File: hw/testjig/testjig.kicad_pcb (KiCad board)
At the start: 2 copper layers, 157.5 x 115.8 mm, 99 parts, among them J1 Conn_02x08_Odd_Even, J10 Conn_01x01, J11 Conn_01x01, J12 Conn_01x01, J13 Conn_01x01, J14 Conn_01x01, J15 Conn_01x01, J16 Conn_01x01, J17 Conn_01x01, J18 Conn_01x01, J19 Conn_01x01, J2 Conn_01x01, J20 Conn_01x04_Female, J21 Conn_01x01, J22 Conn_01x01, J23 Conn_01x01, J24 Conn_01x01, J25 Conn_01x01, J26 Conn_01x01, J27 Conn_01x01, J28 Conn_01x01, J29 Conn_01x01, J3 Conn_01x01, J30 Conn_01x01, J31 Conn_01x01, J32 Conn_01x01, J33 Conn_01x01, J34 Conn_01x01, J35 Conn_01x01, J36 Conn_01x01, J37 Conn_01x01, J38 Conn_01x01, J39 Conn_01x01, J4 Conn_01x01, J40 Conn_01x01, J41 Conn_01x01, J42 Conn_01x01, J43 Conn_02x08_Odd_Even, J44 USB_B_Micro, J45 Conn_02x07_Odd_Even, J46 Conn_01x04_Female, J47 Conn_01x06_Female, J48 Conn_01x02_Female, J49 Conn_01x01, J5 Conn_01x01, J50 Conn_01x01, J51 SJ1-3523N-cap, J6 Conn_01x01, J7 Conn_01x01, J8 Conn_01x01, J9 Conn_01x01, SW1 SW_Push_DPDT, SW2 SW_Push_DPDT, U1 CD74HC4067M

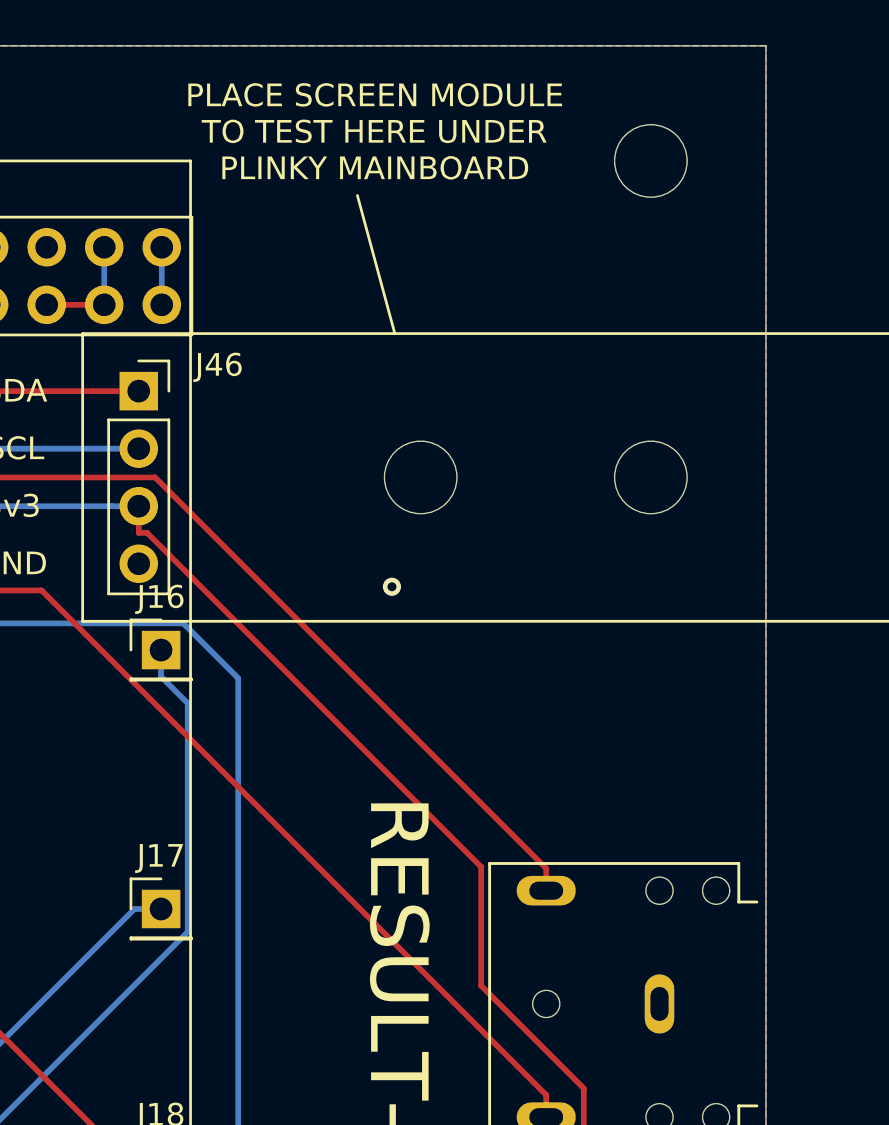
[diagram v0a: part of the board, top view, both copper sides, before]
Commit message: production adjustments and convert testjig to kicad7
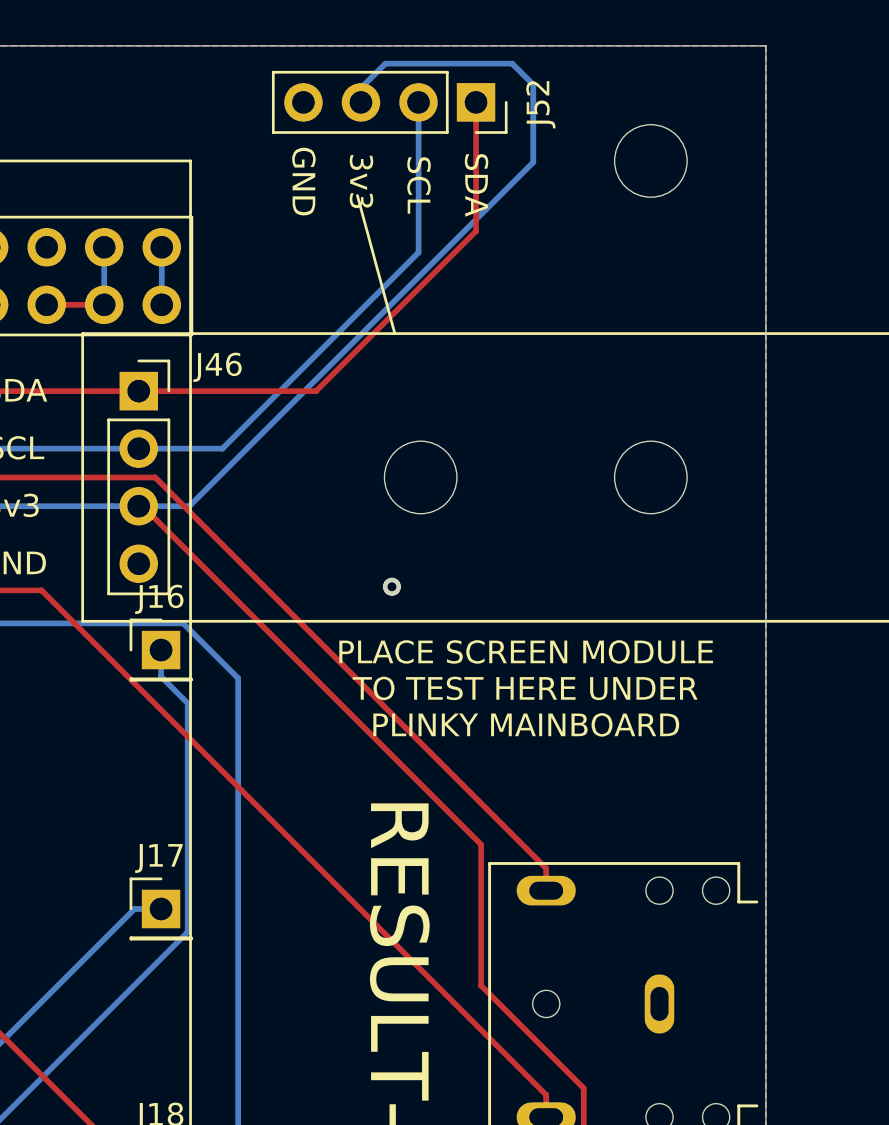
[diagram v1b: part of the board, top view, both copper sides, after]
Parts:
- added J52: Conn_01x04_Female, Connector_PinSocket_2.54mm:PinSocket_1x04_P2.54mm_Vertical, F.Cu at (149.8, 22.8)
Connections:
- J44 pad 4: (no net) -> unconnected-(J44-ID-Pad4)
- J44 pad 6: Net-(J44-Pad6) -> unconnected-(J44-Shield-Pad6)
- J45 pad 1: (no net) -> unconnected-(J45-Pin_1-Pad1)
- J45 pad 10: (no net) -> JTDI
- J45 pad 2: (no net) -> unconnected-(J45-Pin_2-Pad2)
- J45 pad 8: (no net) -> unconnected-(J45-Pin_8-Pad8)
- J45 pad 9: (no net) -> unconnected-(J45-Pin_9-Pad9)
- J47 pad 6: (no net) -> unconnected-(J47-Pin_6-Pad6)
- SW1 pad 3: (no net) -> unconnected-(SW1-C-Pad3)
- SW1 pad 6: (no net) -> unconnected-(SW1-C-Pad6)
- SW2 pad 3: (no net) -> unconnected-(SW2-C-Pad3)
- SW2 pad 6: (no net) -> unconnected-(SW2-C-Pad6)
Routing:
- net +3V3: track 296.0 -> 332.1 mm
- net SDA: track 72.6 -> 96.1 mm
- net SCL: track 72.6 -> 95.2 mm
- net unconnected-(J44-Shield-Pad6): track 0.00 -> 14.1 mm
- net Net-(J44-Pad6): track 14.1 -> 0.00 mm
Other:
- net class Default removed
